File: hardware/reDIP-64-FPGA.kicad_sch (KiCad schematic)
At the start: 23 parts, among them J2 Conn_01x20, J3 Conn_01x20, J4 Conn_01x20, J5 Conn_02x20_Odd_Even, U17 SN74CBT16211ADGVR, U18 SN74CBT16211ADGVR, U19 SN74CBT16211ADGVR, U2 LFE5UM5G-25F-8MG285C, U20 SN74CBT16211ADGVR

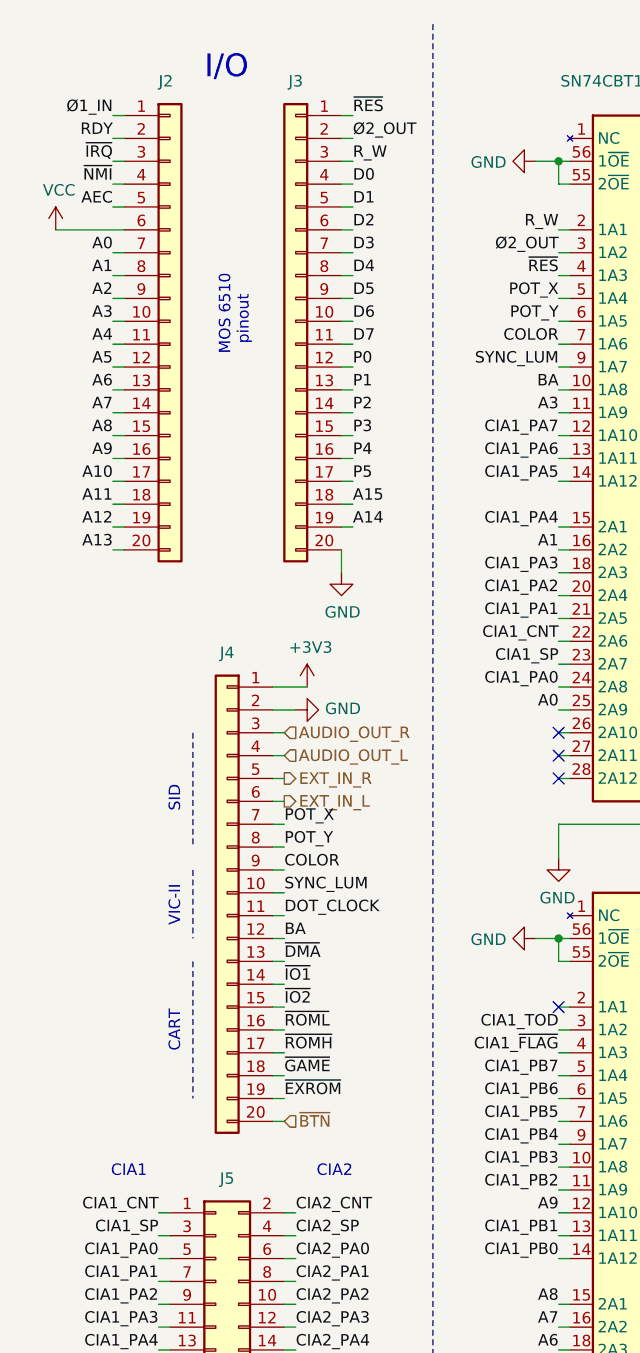
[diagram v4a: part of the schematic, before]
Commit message: Replaced socket pin headers with socket adapter
The socket adapter should hopefully *just* fit.
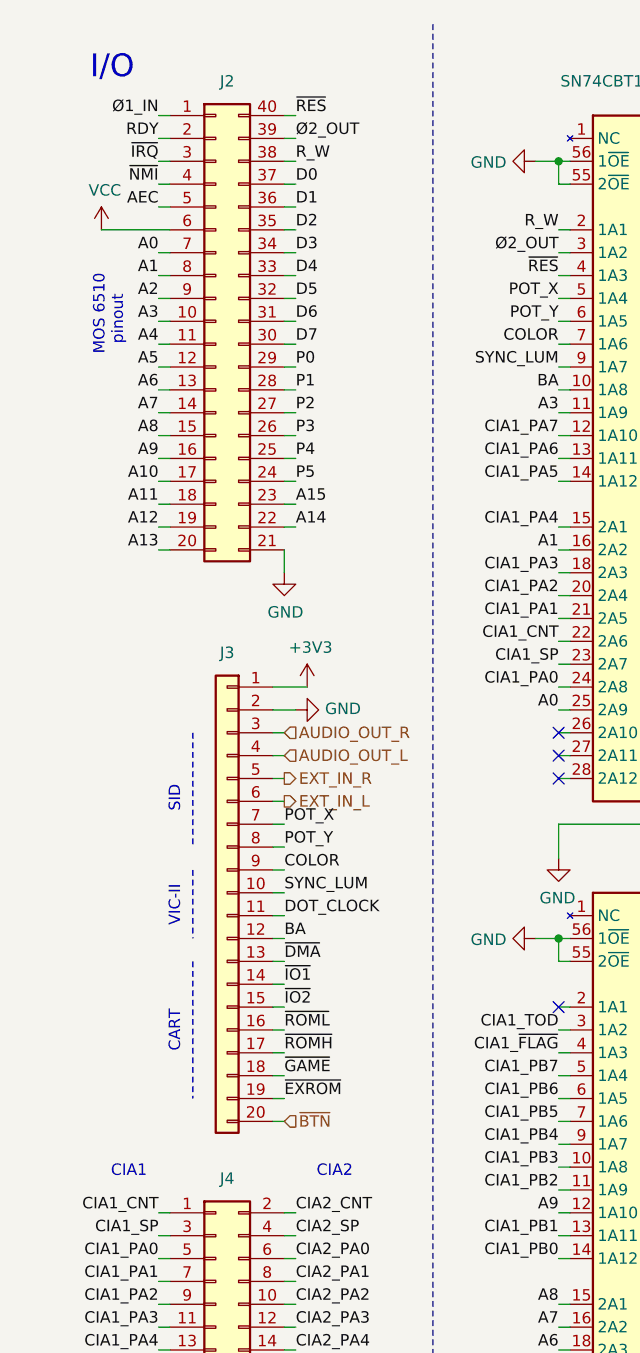
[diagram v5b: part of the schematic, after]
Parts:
- removed J2, J3: Conn_01x20, reDIP:PinHeader_1x20_P2.54mm_Vertical_Machined, symbol Connector_Generic:Conn_01x20
- added J2: Conn_02x20_Counter_Clockwise, reDIP:DIP-40_W15.24mm_Header, symbol Connector_Generic:Conn_02x20_Counter_Clockwise
- renumbered J4 to J3, J5 to J4
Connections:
- net A0: now also J2.7 (Pin_7)
- net A1: now also J2.8 (Pin_8)
- net A10: now also J2.17 (Pin_17)
- net A11: now also J2.18 (Pin_18)
- net A12: now also J2.19 (Pin_19)
- net A13: now also J2.20 (Pin_20)
- net A14: now also J2.22 (Pin_22)
- net A15: now also J2.23 (Pin_23)
- net A2: now also J2.9 (Pin_9)
- net A3: now also J2.10 (Pin_10)
- net A4: now also J2.11 (Pin_11)
- net A5: now also J2.12 (Pin_12)
- net A6: now also J2.13 (Pin_13)
- net A7: now also J2.14 (Pin_14)
- net A8: now also J2.15 (Pin_15)
- net A9: now also J2.16 (Pin_16)
- net AEC: now also J2.5 (Pin_5)
- net D0: now also J2.37 (Pin_37)
- net D1: now also J2.36 (Pin_36)
- net D2: now also J2.35 (Pin_35)
- net D3: now also J2.34 (Pin_34)
- net D4: now also J2.33 (Pin_33)
- net D5: now also J2.32 (Pin_32)
- net D6: now also J2.31 (Pin_31)
- net D7: now also J2.30 (Pin_30)
- net GND: now also J2.21 (Pin_21)
- net P0: now also J2.29 (Pin_29)
- net P1: now also J2.28 (Pin_28)
- net P2: now also J2.27 (Pin_27)
- net P3: now also J2.26 (Pin_26)
- net P4: now also J2.25 (Pin_25)
- net P5: now also J2.24 (Pin_24)
- net RDY: now also J2.2 (Pin_2)
- net R_W: now also J2.38 (Pin_38)
- net VCC: now also J2.6 (Pin_6)
- net ~{IRQ}: now also J2.3 (Pin_3)
- net ~{NMI}: now also J2.4 (Pin_4)
- net ~{RES}: now also J2.40 (Pin_40)
- net Ø1_IN: now also J2.1 (Pin_1)
- net Ø2_OUT: now also J2.39 (Pin_39)

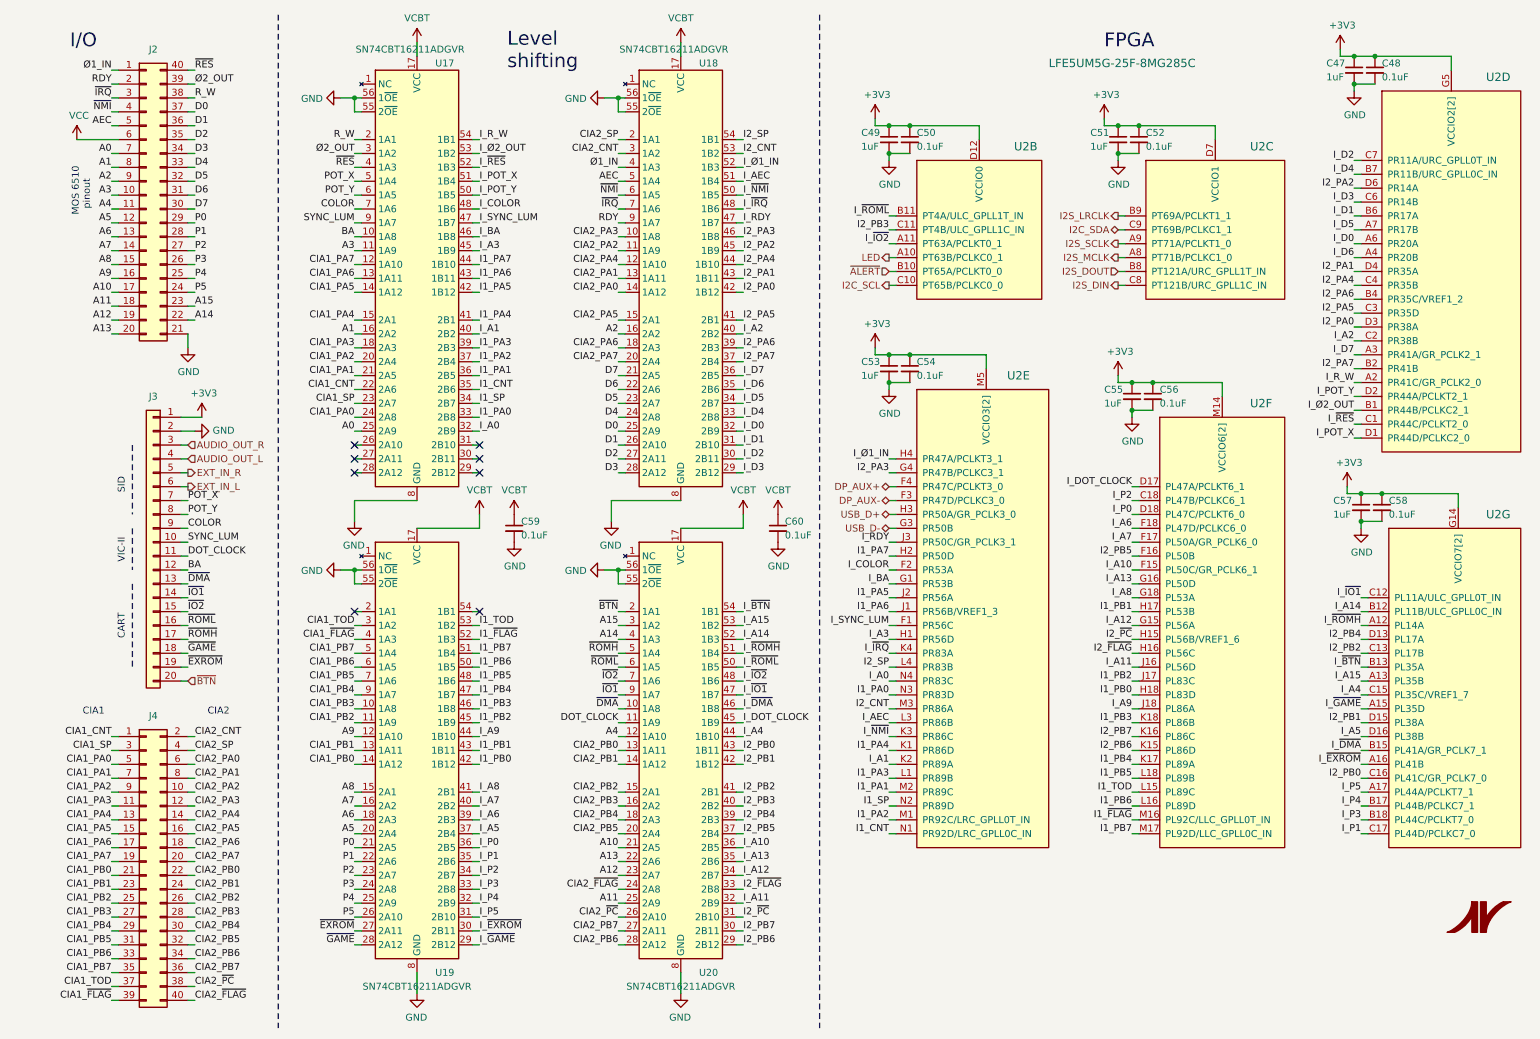
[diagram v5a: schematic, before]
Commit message: A few improvements
* Changed MCLK pullup to 4.7k
* A few pin swaps for cleaner routing
* Example pin headers in BOM
* Replaced reduced lifetime "mobile only" capacitors
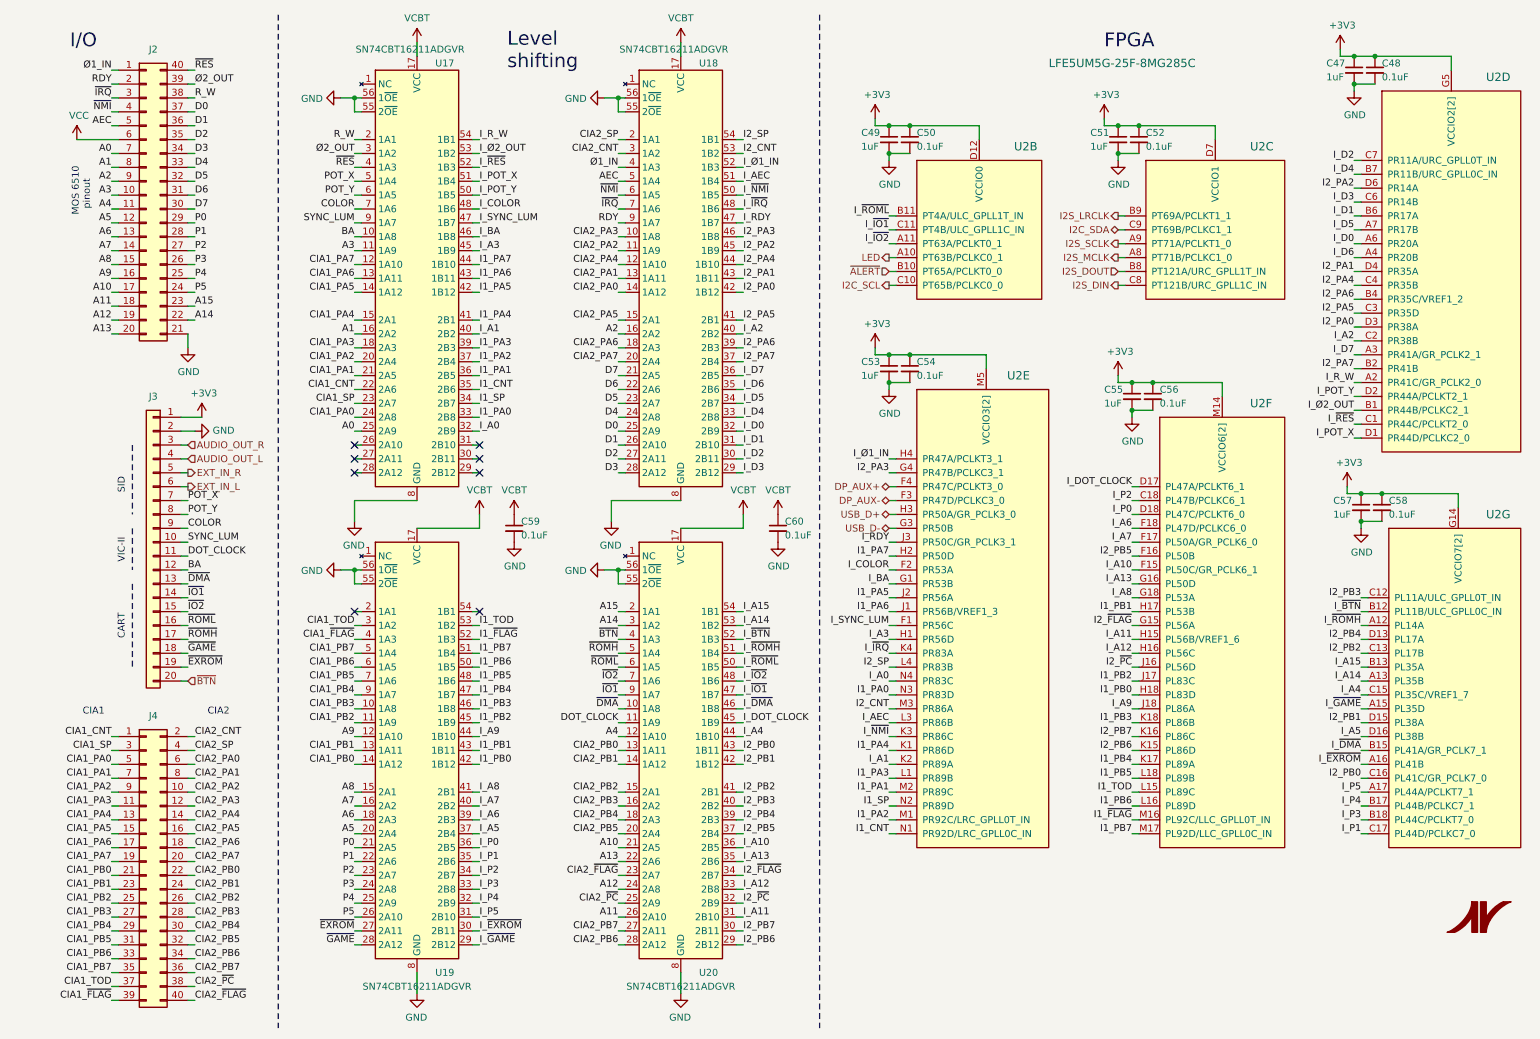
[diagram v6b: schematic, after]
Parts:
- C47, C49, C51, C53, C55, C57: Notes 3.3V DC DERATED TO 1uF -> 3.3V DC DERATED TO 0.7uF; PN GRM035R60J475ME15D -> GRM033R60J225ME01D
- J3: Mfg (none) -> Sullins; PN (none) -> PRPC010SAAN-RC
- J4: Mfg (none) -> Sullins; PN (none) -> PRPC020DAAN-RC
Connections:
- net A11: now also U20.26 (2A10); no longer U20.25 (2A9)
- net A12: now also U20.24 (2A8); no longer U20.23 (2A7)
- net A14: now also U20.3 (1A2); no longer U20.4 (1A3)
- net A15: now also U20.2 (1A1); no longer U20.3 (1A2)
- net CIA2_~{FLAG}: now also U20.23 (2A7); no longer U20.24 (2A8)
- net CIA2_~{PC}: now also U20.25 (2A9); no longer U20.26 (2A10)
- net I2_PB3: now also U2.C12 (PL11A/ULC_GPLL0T_IN); no longer U2.C11 (PT4B/ULC_GPLL1C_IN)
- net I2_~{FLAG}: now also U2.G15 (PL56A), U20.34 (2B7); no longer U2.H16 (PL56C), U20.33 (2B8)
- net I2_~{PC}: now also U2.J16 (PL56D), U20.32 (2B9); no longer U2.H15 (PL56B/VREF1_6), U20.31 (2B10)
- net I_A11: now also U2.H15 (PL56B/VREF1_6), U20.31 (2B10); no longer U2.J16 (PL56D), U20.32 (2B9)
- net I_A12: now also U2.H16 (PL56C), U20.33 (2B8); no longer U2.G15 (PL56A), U20.34 (2B7)
- net I_A14: now also U2.A13 (PL35B), U20.53 (1B2); no longer U2.B12 (PL11B/ULC_GPLL0C_IN), U20.52 (1B3)
- net I_A15: now also U2.B13 (PL35A), U20.54 (1B1); no longer U2.A13 (PL35B), U20.53 (1B2)
- net I_~{BTN}: now also U2.B12 (PL11B/ULC_GPLL0C_IN), U20.52 (1B3); no longer U2.B13 (PL35A), U20.54 (1B1)
- net I_~{IO1}: now also U2.C11 (PT4B/ULC_GPLL1C_IN); no longer U2.C12 (PL11A/ULC_GPLL0T_IN)
- net ~{BTN}: now also U20.4 (1A3); no longer U20.2 (1A1)
